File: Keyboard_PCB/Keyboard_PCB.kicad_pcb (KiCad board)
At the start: 6 copper layers, 120 parts, among them J2 Conn_ARM_SWD_TagConnect_TC2030, J3 CH_USB_C, SW1 BOOT, SW10 7, SW11 8, SW12 9, SW13 10, SW14 11, SW15 EC11E15244G1, SW2 NRST, SW3 0, SW4 1, SW5 2, SW6 3, SW7 4, SW8 5, SW9 6, U1 S40FC002C1B2I00000, U2 STM32U385VGI6, U3 CC2500, U4 2450BM15B0003001E, U5 USBLC6-2SC6, U6 ISL91127IRAZ, U7 MCP73833, Y1 26MHz, Y2 25MHz, Y3 32.786KHz

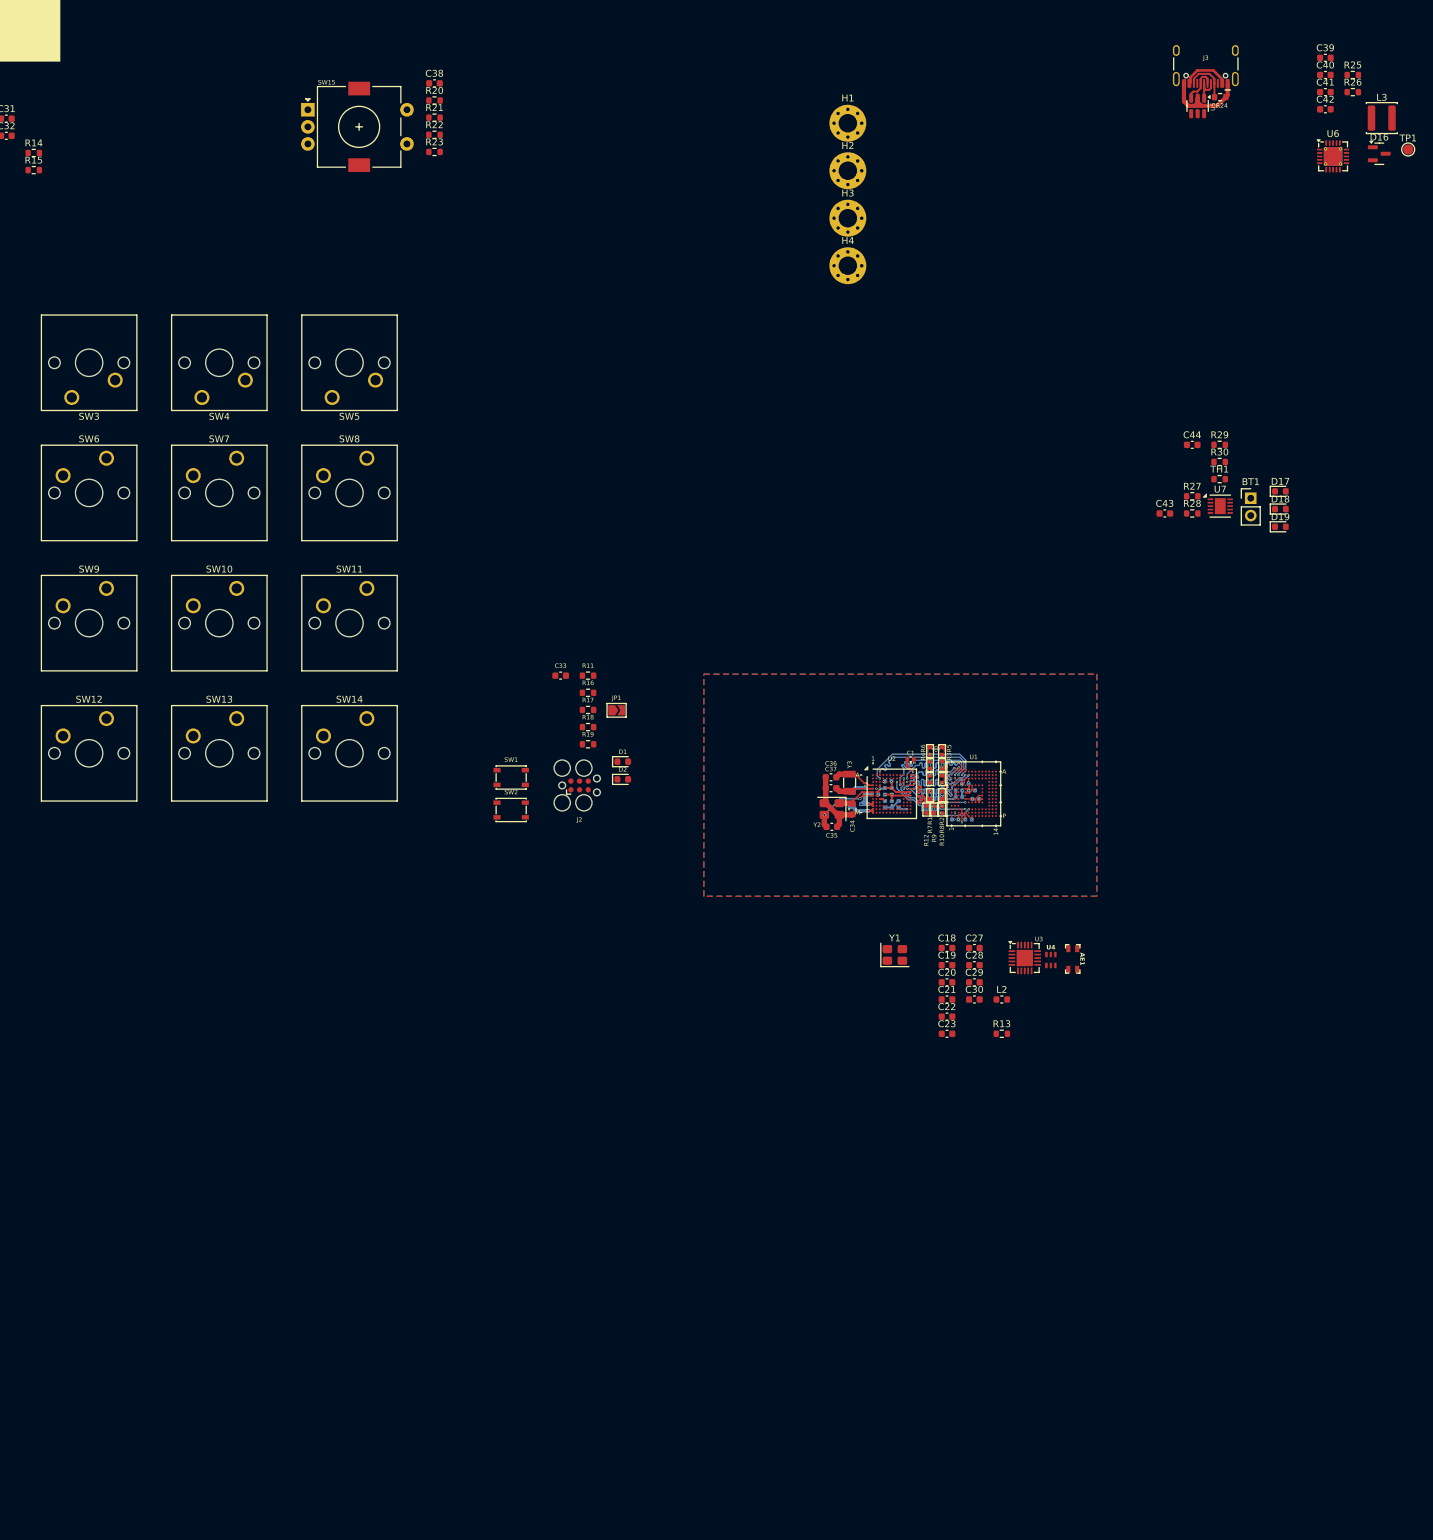
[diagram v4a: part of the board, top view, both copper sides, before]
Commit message: Buck and bat routing
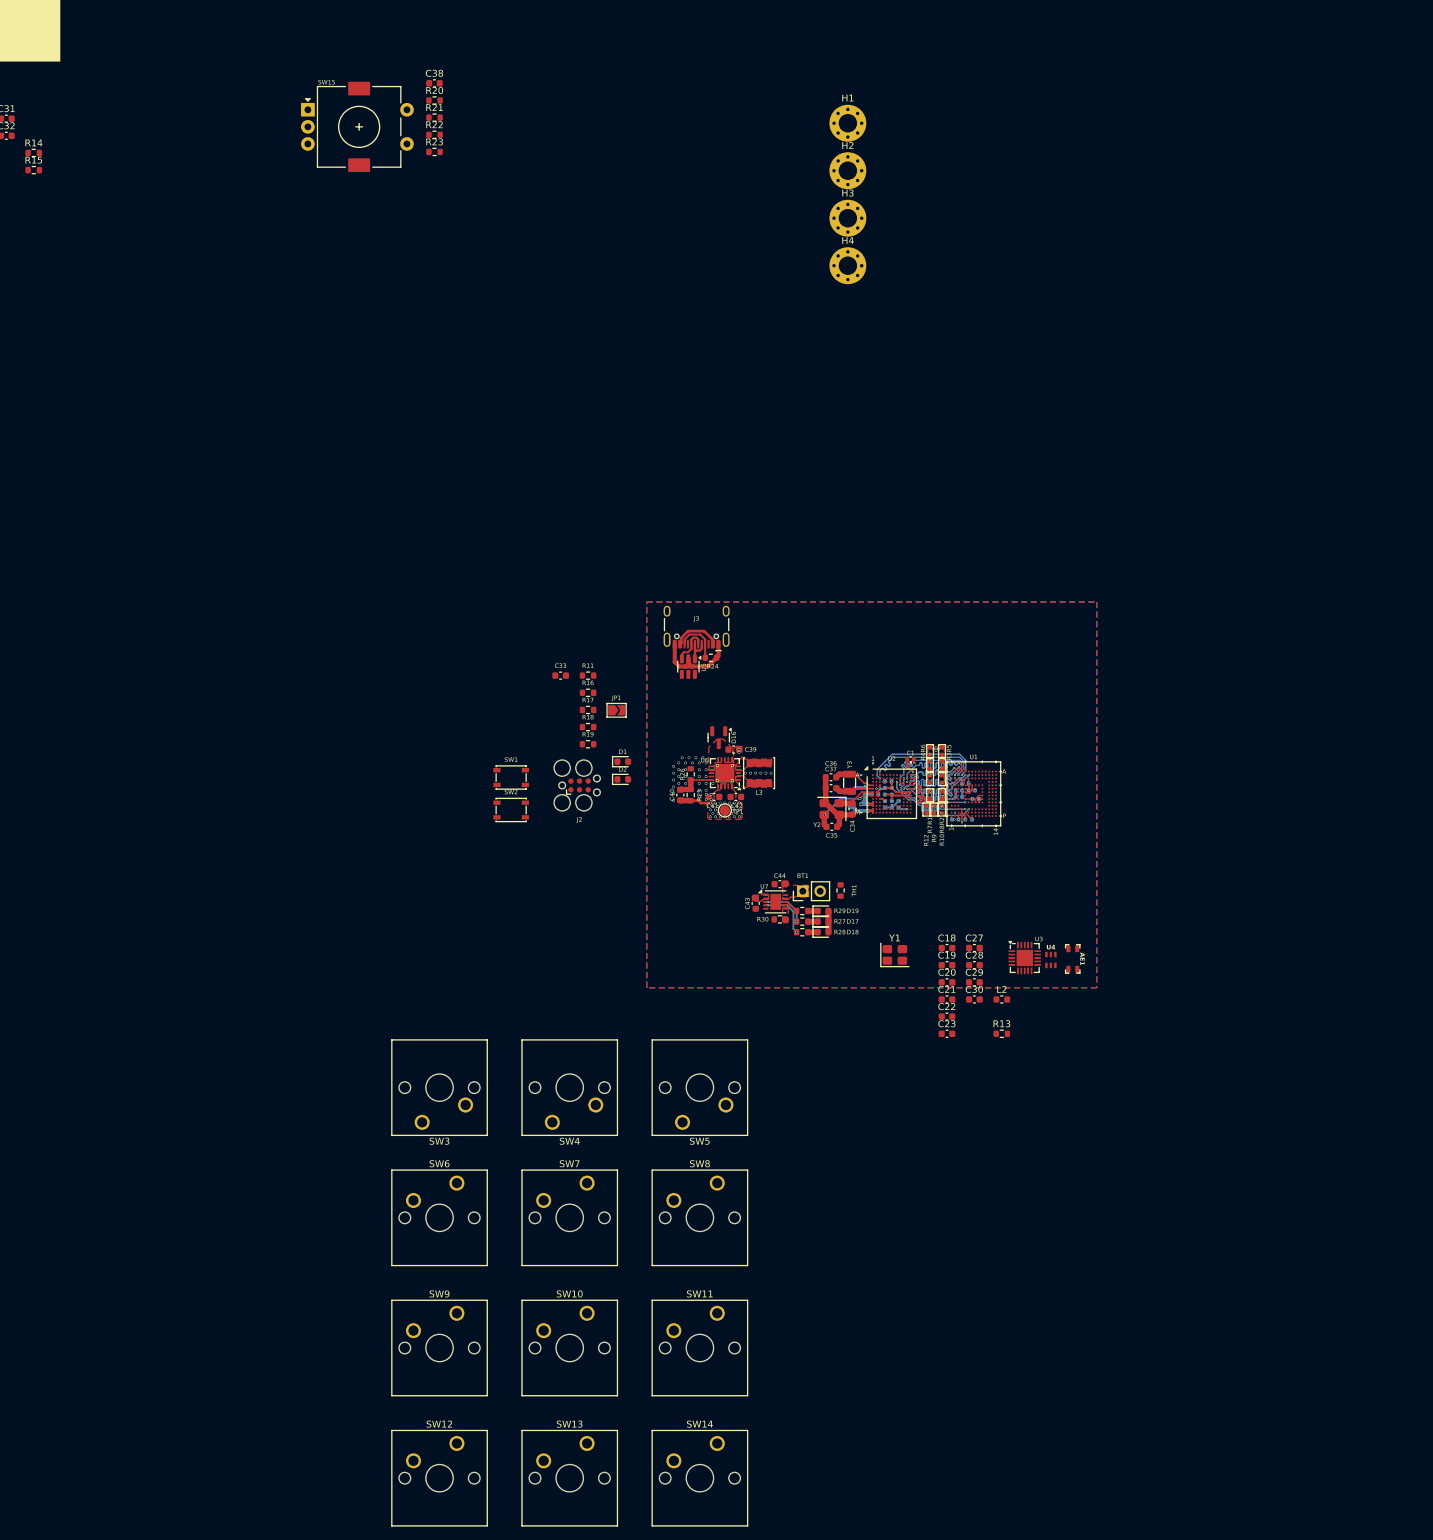
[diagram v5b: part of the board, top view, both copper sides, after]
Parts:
- moved R25 143.1 mm to (191.3, 158.9), turned to 90 degrees
- moved C40 141.5 mm to (189.8, 158.9), turned to 90 degrees
- moved R26 139.1 mm to (191.3, 155.9), turned to -90 degrees
- moved TP1 139.1 mm to (196.3, 161.1)
- moved C41 136.5 mm to (194.7, 159.2), turned to 180 degrees
- moved C39 133.2 mm to (197.6, 152.2)
- moved C42 132.5 mm to (197.9, 159.2)
- moved L3 132.3 mm to (201.3, 155.7), turned to -90 degrees
- moved D16 129.0 mm to (195.4, 150.5), turned to -90 degrees
- moved U6 126.8 mm to (196.3, 155.7), turned to 180 degrees
- moved SW12 117.8 mm to (157.1, 253.8)
- moved SW14 117.8 mm to (195.2, 253.8)
- moved SW6 117.8 mm to (157.1, 215.7)
- moved SW8 117.8 mm to (195.2, 215.7)
- moved SW13 117.8 mm to (176.2, 253.8)
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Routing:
- net Net-(U7-STAT2): track 0.00 -> 7.63 mm, vias 0 -> 2
- net Net-(U7-STAT1): track 0.00 -> 6.63 mm, vias 0 -> 2
- net Net-(U6-FB): track 0.00 -> 5.97 mm
- net +3V3: track 15.9 -> 20.4 mm, vias 14 -> 40
- net /PWR/VBUS: track 7.17 -> 10.3 mm
- net GND: track 55.1 -> 57.5 mm, vias 17 -> 60
- net Net-(U7-~{PG}): track 0.00 -> 1.99 mm
- net Net-(D19-K): track 0.00 -> 1.44 mm
- net Net-(D18-K): track 0.00 -> 1.44 mm
- net Net-(D17-K): track 0.00 -> 1.44 mm
- added copper zone on F.Cu, net /BAT
- added copper zone on F.Cu, net /PWR/BAT_PROG
- added copper zone on F.Cu, net /PWR/VBUS
- added copper zone on F.Cu, net Net-(L3-Pad1)
- added copper zone on F.Cu, net Net-(L3-Pad2)
- added copper zone on F.Cu, net Net-(U6-EN)

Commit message: Layout progress
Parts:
- C1, C24, C26, C31, C32, C34, C35, C36, C37, R1, R10, R12, R14, R15, R2, R21, R23, R3, R4, R5, R6, R7, R8, R9, U1, U2, U3, Y2, Y3: moved to B.Cu
- C10, C11, C12, C13, C14, C15, C16, C17, C2, C25, C3, C4, C5, C6, C7, C8, C9, L1: moved to F.Cu
- L2: footprint Inductor_SMD:L_0603_1608Metric -> Inductor_SMD:L_0402_1005Metric
- moved J1 228.1 mm to (283.4, 163.1)
- moved C32 220.1 mm to (287.1, 162.6), turned to -90 degrees
- moved C31 219.8 mm to (285.6, 162.6), turned to -90 degrees
- moved C26 216.0 mm to (281.1, 162.6), turned to 90 degrees
- moved C24 215.8 mm to (279.6, 162.6), turned to -90 degrees
- moved R15 212.5 mm to (286.4, 160.3)
- moved R14 210.4 mm to (282.8, 160.3)
- moved H3 169.9 mm to (183.3, 241.5)
- moved H4 162.2 mm to (240.3, 241.5)
- moved C38 131.4 mm to (253.9, 139.9)
- moved R20 131.4 mm to (253.9, 142.4)
- moved R22 131.4 mm to (253.9, 147.5)
- moved SW15 123.4 mm to (220.9, 147.5)
- moved R23 112.2 mm to (220.9, 154.7)
- moved R21 108.8 mm to (220.9, 145.4)
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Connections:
- net Net-(U3-RF_N) renamed /RF_N
- net Net-(U3-RF_P) renamed /RF_P
- C11 pad 2: VCC_q -> +3V3
- C12 pad 2: VCC -> +3V3
- C13 pad 2: VCC_q -> +3V3
- C14 pad 2: /VCCI -> +3V3
- C15 pad 2: VCC -> +3V3
- C16 pad 2: VCC_q -> +3V3
- C17 pad 2: /VCCI -> +3V3
- U1 pad C2: /VCCI -> +3V3
- U1 pad C6: VCC_q -> +3V3
- U1 pad E6: VCC -> +3V3
- U1 pad F5: VCC -> +3V3
- U1 pad J10: VCC -> +3V3
- U1 pad K9: VCC -> +3V3
- U1 pad M4: VCC_q -> +3V3
- U1 pad N4: VCC_q -> +3V3
- U1 pad P3: VCC_q -> +3V3
- U1 pad P5: VCC_q -> +3V3
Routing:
- net +3V3: track 20.4 -> 31.2 mm, vias 40 -> 51
- net Net-(U7-~{PG}): track 1.99 -> 10.4 mm, vias 0 -> 2
- net Net-(U6-FB): track 5.97 -> 0.00 mm
- net VCC: track 3.88 -> 0.00 mm, vias 2 -> 0
- net VCC_q: track 3.43 -> 0.00 mm, vias 3 -> 0
- net /VCCI: track 3.21 -> 0.00 mm, vias 2 -> 0
- net GND: track 57.5 -> 54.4 mm, vias 60 -> 45
- net Net-(U7-STAT1): track 6.63 -> 8.78 mm
- net Net-(C26-Pad1): track 0.00 -> 1.77 mm, vias 0 -> 1
- net Net-(C24-Pad2): track 0.00 -> 1.77 mm, vias 0 -> 1
- net Net-(J1-Pad13): track 0.00 -> 1.56 mm, vias 0 -> 1
- net /OLED_RST: track 0.00 -> 1.50 mm, vias 0 -> 1
- net Net-(D19-K): track 1.44 -> 0.00 mm
- net Net-(D18-K): track 1.44 -> 0.00 mm
- net Net-(D17-K): track 1.44 -> 0.00 mm
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- added copper zone on B.Cu, net +3V3
- added copper zone on F.Cu, net Net-(D1-A)
- added copper zone on F.Cu, net Net-(D17-K)
- added copper zone on F.Cu, net Net-(D18-K)
- added copper zone on F.Cu, net Net-(D19-K)
- added copper zone on F.Cu, net Net-(D2-A)
- added copper zone on F.Cu, net Net-(JP1-B)
- added copper zone on F.Cu, net Net-(U6-FB)
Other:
- board outline added: 65 x 103 mm
- board text added: "cable length: 25 - 4.5 mm"

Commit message: Layout progress
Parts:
- AE1, C18, C19, C20, C21, C22, C23, C27, C28, C29, C30, J1, L2, R13, TH1, U4, Y1: moved to B.Cu
- moved R15 82.9 mm to (203.7, 166.3), turned to -90 degrees
- moved C24 81.5 mm to (198.1, 166.3)
- moved C26 81.5 mm to (199.7, 166.3), turned to -90 degrees
- moved C32 81.3 mm to (206.0, 167.0), turned to 0 degrees
- moved J1 80.9 mm to (202.4, 162.9)
- moved R14 80.9 mm to (202.1, 166.3), turned to 90 degrees
- moved C31 79.7 mm to (206.0, 165.5), turned to 0 degrees
- moved TH1 69.1 mm to (211.8, 202.9), turned to 0 degrees
- moved C27 63.1 mm to (232.9, 148.6), turned to 180 degrees
- moved U4 53.0 mm to (229.9, 148.6), turned to 90 degrees
- moved L2 52.3 mm to (229.9, 150.6)
- moved C18 45.2 mm to (241.3, 126.8), turned to 180 degrees
- moved C21 45.2 mm to (241.3, 134.3), turned to 180 degrees
- moved C19 45.2 mm to (241.3, 129.3), turned to 180 degrees
- moved C20 45.2 mm to (241.3, 131.8), turned to 180 degrees
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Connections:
- net Net-(U4-CAP) renamed /RF_CAP
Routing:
- net Net-(AE1-FEED): track 0.00 -> 6.92 mm
- net /RF_P: track 0.00 -> 3.36 mm
- net /RF_N: track 0.00 -> 3.35 mm
- net Net-(C26-Pad2): track 0.00 -> 3.29 mm, vias 1 -> 0
- net /BAT: track 0.00 -> 2.81 mm
- net Net-(C32-Pad1): track 0.81 -> 3.28 mm, vias 1 -> 0
- net Net-(C24-Pad2): track 1.77 -> 3.30 mm, vias 1 -> 0
- net Net-(C24-Pad1): track 0.03 -> 1.54 mm, vias 1 -> 0
- net +3V3: track 31.2 -> 29.7 mm
- net /RF_CAP: track 0.00 -> 1.41 mm
- net Net-(C31-Pad1): track 0.81 -> 1.33 mm, vias 1 -> 0
- net Net-(C26-Pad1): track 1.77 -> 1.30 mm, vias 1 -> 0
- net Net-(J1-Pad13): track 1.56 -> 1.89 mm, vias 1 -> 0
- net GND: vias 45 -> 67
- net /OLED_RST: track 1.50 -> 1.49 mm, vias 1 -> 0
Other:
- board text added: "FOLD"
- board text removed: "cable length: 25 - 4.5 mm"

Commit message: RF layout progress
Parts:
- removed C22: 220p, Capacitor_SMD:C_0603_1608Metric
- moved R13 59.4 mm to (235.2, 155.3), turned to 90 degrees
- moved C29 48.7 mm to (227.7, 157.9), turned to -90 degrees
- moved C30 44.0 mm to (224.8, 155.0)
- moved Y1 40.6 mm to (224.8, 157.6)
- moved C28 30.0 mm to (229.3, 158.2), turned to 90 degrees
- moved C18 29.5 mm to (233.7, 155.3), turned to 90 degrees
- moved C19 27.3 mm to (226.0, 152.0), turned to 0 degrees
- moved C21 24.5 mm to (226.0, 153.5), turned to 0 degrees
- moved C23 21.5 mm to (230.8, 158.2), turned to 90 degrees
- moved C20 20.7 mm to (233.2, 150.9)
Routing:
- net +3V3: track 29.7 -> 39.1 mm, vias 51 -> 56
- net Net-(U3-XOSC_Q1): track 0.00 -> 8.40 mm, vias 0 -> 2
- net Net-(U3-XOSC_Q2): track 0.00 -> 7.01 mm, vias 0 -> 2
- net Net-(U3-RBIAS): track 0.00 -> 3.56 mm
- net GND: track 54.4 -> 50.9 mm, vias 67 -> 101
- net Net-(U3-DCOUPL): track 0.00 -> 1.58 mm
